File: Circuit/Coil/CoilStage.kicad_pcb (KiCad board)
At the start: 2 copper layers, 48.3 x 33 mm, 10 parts, among them J1 Coil Power, J2 Trigger, Q1 TIC126

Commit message: [Circuit] Optimize a PCB design
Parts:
- moved D3 7.62 mm to (114.3, 74.9)
- moved L1 3.81 mm to (123.2, 80.0)
- moved Q1 3.81 mm to (118.1, 67.3)
- moved J1 1.27 mm to (81.3, 81.3)
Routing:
- net /TriggerSignal: track 15.5 -> 8.67 mm
- net Net-(D3-Pad1): track 8.67 -> 4.86 mm
- net Net-(C1-Pad1): track 36.7 -> 40.5 mm
- net GND: track 70.0 -> 66.5 mm
- net Net-(D4-Pad1): track 24.2 -> 22.6 mm
- net /CoilPower+: track 11.4 -> 10.2 mm
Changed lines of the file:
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@@
     (thickness 1.6)
     (drawings 4)
-    (tracks 26)
+    (tracks 23)
     (zones 0)
     (modules 10)
@@
   )
   (module Package_TO_SOT_THT:TO-220-3_Vertical (layer F.Cu)
-    (at 114.3 67.31 270)
+    (at 118.11 67.31 270)
     (descr "TO-220-3, Vertical, RM 2.54mm, see https://www.vishay.com/docs/66542/to-220-1.pdf")
     (tags "TO-220-3 Vertical RM 2.54mm")
@@
   )
   (module TestPoint:TestPoint_2Pads_Pitch5.08mm_Drill1.3mm (layer F.Cu)
-    (at 119.38 80.01 180)
+    (at 123.19 80.01 180)
     (descr "Test point with 2 pads, pitch 5.08mm, hole diameter 1.3mm, wire diameter 1.0mm")
     (tags "CONN DEV")
@@
   )
   (module TerminalBlock:TerminalBlock_bornier-2_P5.08mm (layer F.Cu)
-    (at 81.28 82.55 270)
+    (at 81.28 81.28 270)
     (descr "simple 2-pin terminal block, pitch 5.08mm, revamped version of bornier2")
     (tags "terminal block bornier2")
@@
   )
   (module Diode_THT:D_DO-41_SOD81_P10.16mm_Horizontal (layer F.Cu)
-    (at 121.92 74.93 90)
+    (at 114.3 74.93 90)
     (descr "Diode, DO-41_SOD81 series, Axial, Horizontal, pin pitch=10.16mm, , length*diameter=5.2*2.7mm^2, , http://www.diodes.com/_files/packages/DO-41%20(Plastic).pdf")
     (tags "Diode DO-41_SOD81 series Axial Horizontal pin pitch 10.16mm  length 5.2mm diameter 2.7mm")
@@
   (gr_line (start 125.73 58.42) (end 125.73 91.44) (layer Edge.Cuts) (width 0.1))
   (gr_line (start 77.47 58.42) (end 125.73 58.42) (layer Edge.Cuts) (width 0.1))
-  (segment (start 90.01 87.63) (end 97.79 79.85) (width 0.25) (layer B.Cu) (net 1) (status 20))
-  (segment (start 81.28 87.63) (end 90.01 87.63) (width 0.25) (layer B.Cu) (net 1) (status 10))
   (segment (start 103.98 79.85) (end 110.49 86.36) (width 2) (layer B.Cu) (net 1) (status 20))
   (segment (start 97.79 79.85) (end 103.98 79.85) (width 2) (layer B.Cu) (net 1) (status 10))
-  (segment (start 114.3 82.55) (end 114.3 80.01) (width 2) (layer B.Cu) (net 1) (status 20))
-  (segment (start 110.49 86.36) (end 114.3 82.55) (width 2) (layer B.Cu) (net 1) (status 10))
-  (segment (start 114.3 80.01) (end 116.84 77.47) (width 0.25) (layer F.Cu) (net 1))
-  (segment (start 123.19 77.47) (end 124.46 76.2) (width 0.25) (layer F.Cu) (net 1))
-  (segment (start 124.46 76.2) (end 124.46 60.96) (width 0.25) (layer F.Cu) (net 1))
-  (segment (start 116.84 77.47) (end 123.19 77.47) (width 0.25) (layer F.Cu) (net 1))
+  (segment (start 124.46 73.66) (end 124.46 60.96) (width 0.25) (layer F.Cu) (net 1) (status 20))
+  (segment (start 111.76 86.36) (end 118.11 80.01) (width 2) (layer B.Cu) (net 1) (status 30))
+  (segment (start 110.49 86.36) (end 111.76 86.36) (width 2) (layer B.Cu) (net 1) (status 30))
+  (segment (start 118.11 80.01) (end 124.46 73.66) (width 0.25) (layer F.Cu) (net 1) (status 10))
+  (segment (start 91.28 86.36) (end 91.36 86.28) (width 0.25) (layer B.Cu) (net 1))
+  (segment (start 81.28 86.36) (end 91.28 86.36) (width 0.25) (layer B.Cu) (net 1))
+  (segment (start 91.36 86.28) (end 97.79 79.85) (width 0.25) (layer B.Cu) (net 1))
   (segment (start 88.9 60.96) (end 97.79 69.85) (width 0.25) (layer B.Cu) (net 2) (status 20))
   (segment (start 81.28 60.96) (end 88.9 60.96) (width 0.25) (layer B.Cu) (net 2) (status 10))
-  (segment (start 114.3 69.85) (end 97.79 69.85) (width 2) (layer B.Cu) (net 2))
-  (segment (start 81.28 82.55) (end 81.28 71.12) (width 0.25) (layer B.Cu) (net 3) (status 30))
+  (segment (start 97.79 69.85) (end 118.11 69.85) (width 2) (layer B.Cu) (net 2) (status 30))
+  (segment (start 81.28 71.12) (end 81.28 81.28) (width 0.25) (layer B.Cu) (net 3))
   (segment (start 119.38 60.96) (end 121.92 60.96) (width 0.25) (layer B.Cu) (net 4) (status 30))
   (segment (start 107.95 60.96) (end 111.76 60.96) (width 0.25) (layer B.Cu) (net 5) (status 30))
-  (segment (start 115.57 64.77) (end 111.76 60.96) (width 0.25) (layer B.Cu) (net 5))
-  (segment (start 121.92 64.77) (end 115.57 64.77) (width 0.25) (layer B.Cu) (net 5))
-  (segment (start 119.38 72.39) (end 121.92 74.93) (width 0.25) (layer F.Cu) (net 6))
-  (segment (start 114.3 72.39) (end 119.38 72.39) (width 0.25) (layer F.Cu) (net 6))
-  (segment (start 123.19 83.82) (end 119.38 80.01) (width 2) (layer B.Cu) (net 7) (status 20))
-  (segment (start 123.19 86.36) (end 123.19 83.82) (width 2) (layer B.Cu) (net 7) (status 10))
-  (segment (start 116.84 67.31) (end 119.38 69.85) (width 2) (layer B.Cu) (net 7))
-  (segment (start 114.3 67.31) (end 116.84 67.31) (width 2) (layer B.Cu) (net 7) (status 10))
-  (segment (start 119.38 72.39) (end 119.38 80.01) (width 2) (layer B.Cu) (net 7) (status 20))
-  (segment (start 119.38 69.85) (end 119.38 72.39) (width 2) (layer B.Cu) (net 7))
+  (segment (start 114.3 63.5) (end 111.76 60.96) (width 0.25) (layer B.Cu) (net 5) (status 20))
+  (segment (start 114.3 64.77) (end 114.3 63.5) (width 0.25) (layer B.Cu) (net 5) (status 10))
+  (segment (start 115.57 74.93) (end 118.11 72.39) (width 0.25) (layer B.Cu) (net 6) (status 20))
+  (segment (start 114.3 74.93) (end 115.57 74.93) (width 0.25) (layer B.Cu) (net 6) (status 10))
+  (segment (start 123.19 86.36) (end 123.19 80.01) (width 2) (layer B.Cu) (net 7) (status 30))
+  (segment (start 123.19 80.01) (end 123.19 69.85) (width 2) (layer B.Cu) (net 7) (status 10))
+  (segment (start 120.65 67.31) (end 118.11 67.31) (width 2) (layer B.Cu) (net 7) (status 20))
+  (segment (start 123.19 69.85) (end 120.65 67.31) (width 2) (layer B.Cu) (net 7))
 )

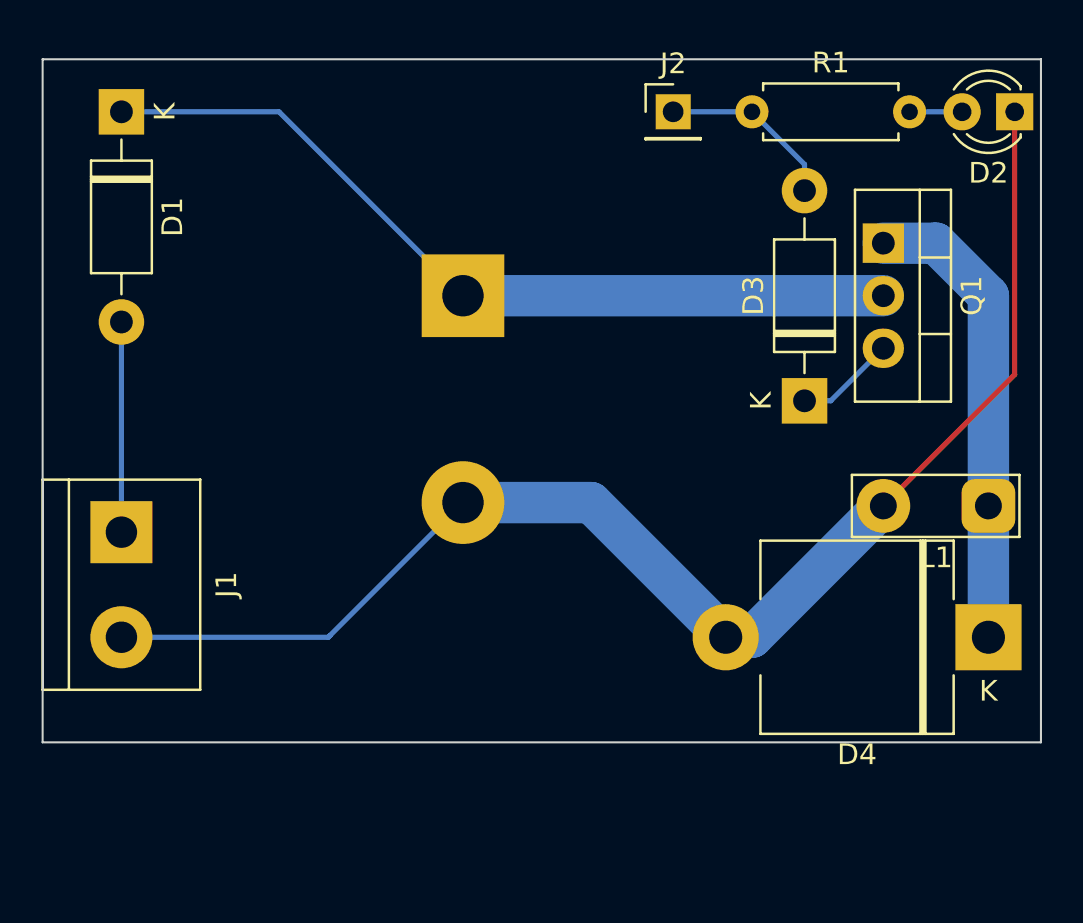
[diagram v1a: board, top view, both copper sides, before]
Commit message: [Circuit] Use a bigger SCR
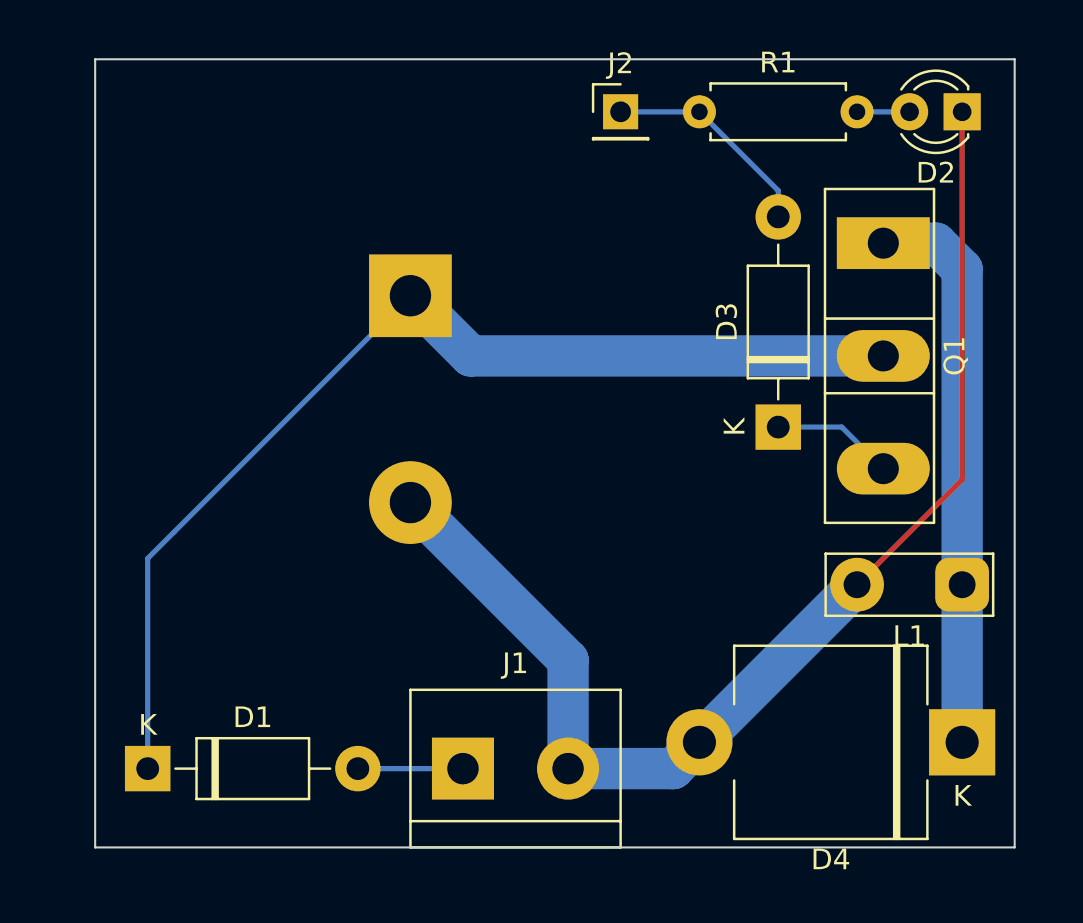
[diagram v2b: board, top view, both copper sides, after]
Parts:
- Q1: value TIC126 -> 70PT12DS; footprint Package_TO_SOT_THT:TO-220-3_Vertical -> Package_TO_SOT_THT:TO-247-3_Vertical
- moved D1 31.8 mm to (82.5, 92.7), turned to 0 degrees
- moved J1 20.1 mm to (97.8, 92.7), turned to 0 degrees
- moved D4 5.24 mm to (121.9, 91.4)
- moved L1 4.02 mm to (121.9, 83.8)
- moved C1 2.54 mm to (95.2, 69.8)
- moved J2 2.54 mm to (105.4, 61.0)
- moved R1 2.54 mm to (109.2, 61.0)
- moved D2 2.54 mm to (121.9, 61.0)
- moved D3 1.80 mm to (113.0, 76.2)
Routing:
- net Net-(C1-Pad1): track 40.5 -> 52.2 mm
- net GND: track 66.5 -> 58.6 mm
- net /CoilPower+: track 10.2 -> 5.08 mm
- net Net-(D4-Pad1): track 22.6 -> 27.2 mm
- net /TriggerSignal: track 8.67 -> 10.5 mm
- net Net-(D3-Pad1): track 4.86 -> 5.91 mm
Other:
- board size 48.3 x 33 mm -> 44.4 x 38.1 mm

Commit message: [Circuit] Update circuit files to KiCAD 6's
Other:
- net class Default removed
